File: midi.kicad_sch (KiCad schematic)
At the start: 9 parts, among them J7 MIDI Out 1, J8 MIDI In 1

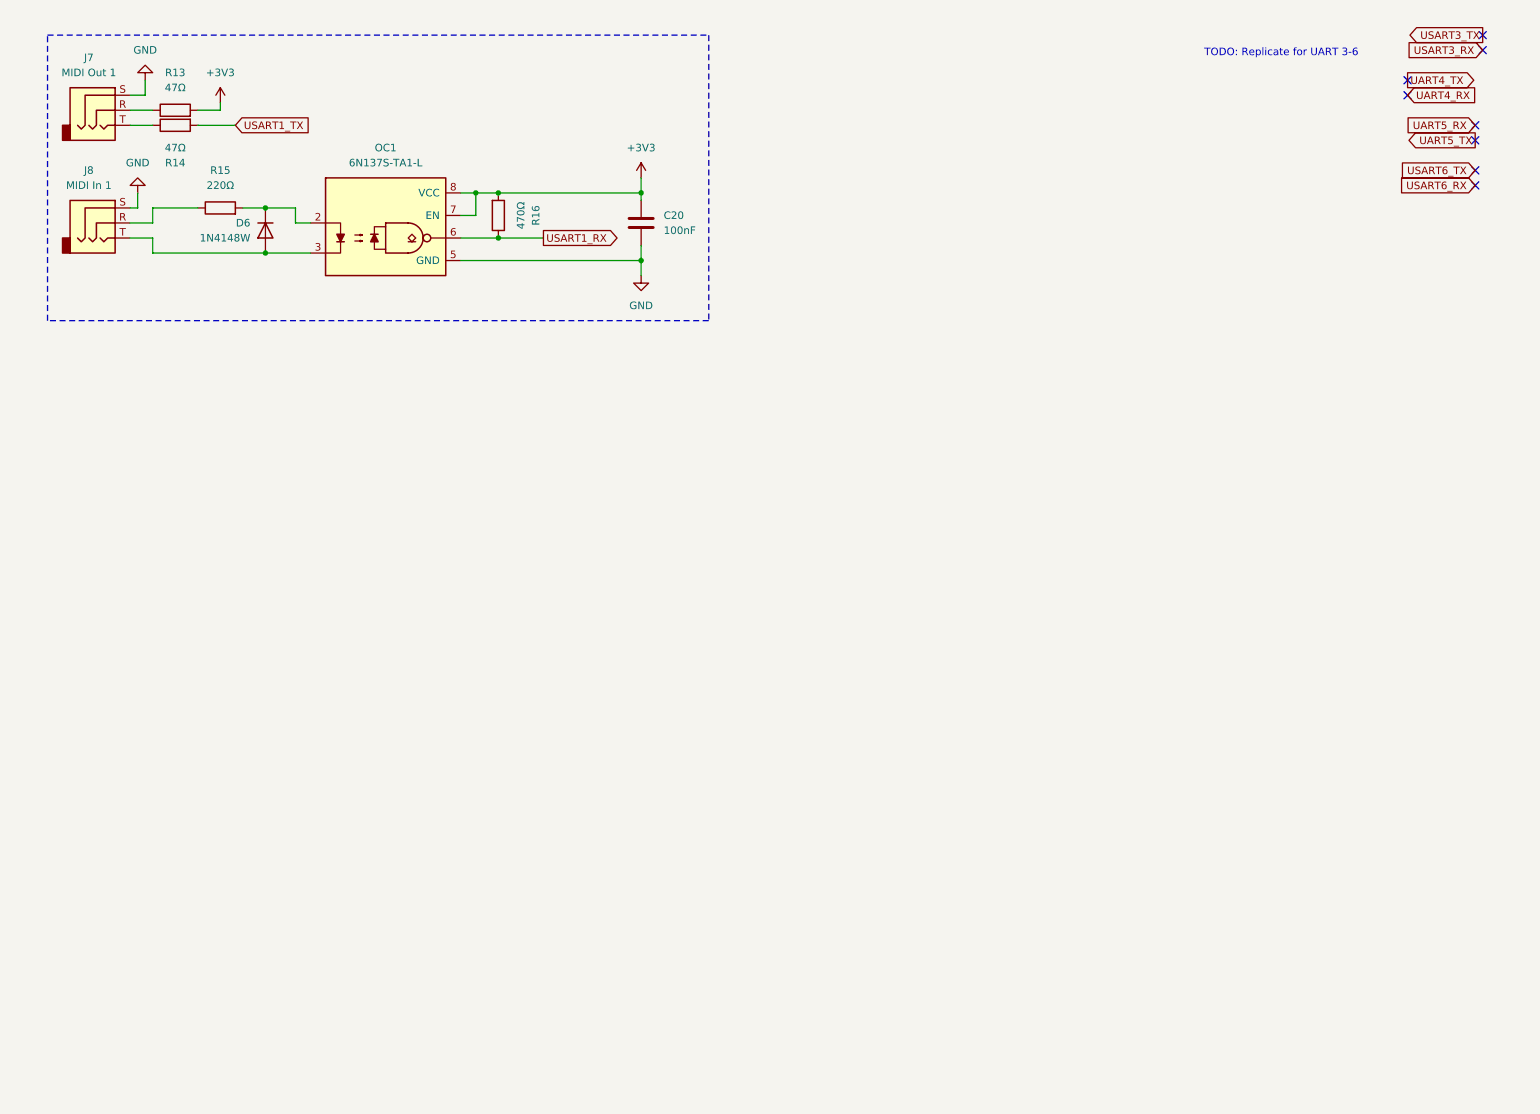
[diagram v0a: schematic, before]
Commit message: Updated schematic with parts found in JLCPCB parts database. Updated footprints, 3d models for those items. All schematic symbols now have LCSC part numbers, footprints and 3D models. No PCB layout has been done.
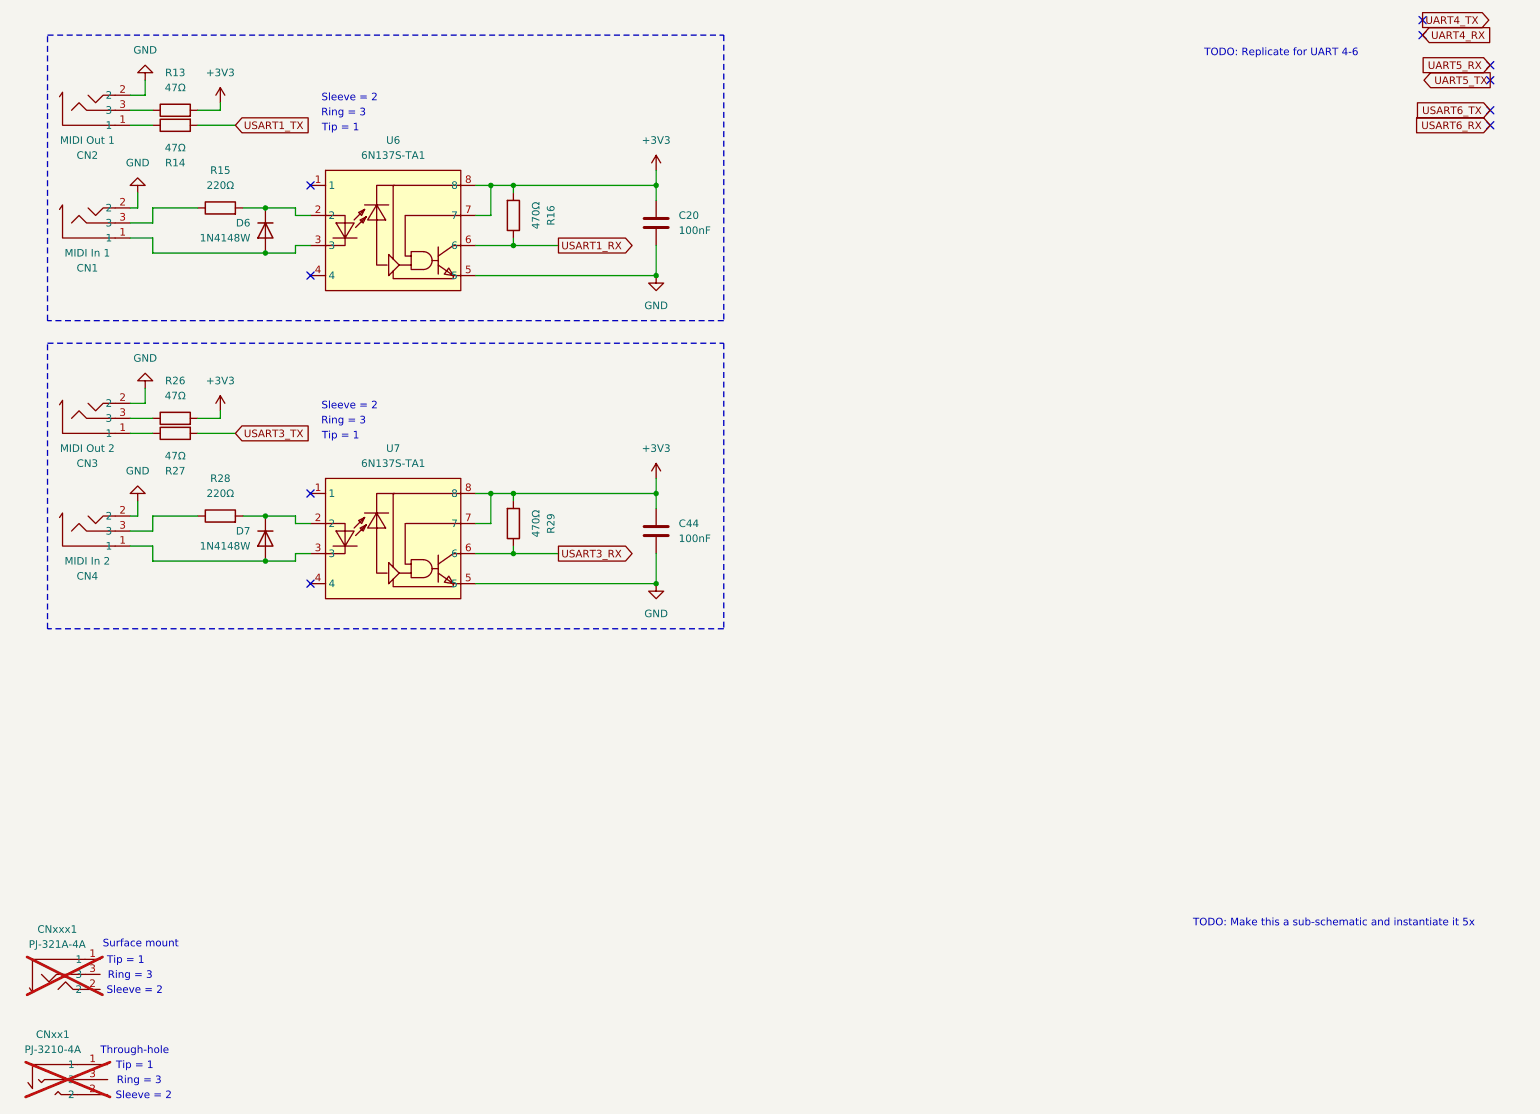
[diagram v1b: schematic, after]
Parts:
- removed J7: MIDI Out 1, symbol Connector_Audio:AudioJack3
- removed J8: MIDI In 1, symbol Connector_Audio:AudioJack3
- removed OC1: 6N137S-TA1-L, PCM_Package_DIP_AKL:SMDIP-8_W9.53mm, symbol PCM_Optocoupler_Logic_AKL:6N137-X007T
- added C44: 100nF, Capacitor_SMD:C_0402_1005Metric, symbol Device:C
- added CN1: MIDI In 1, easyeda2kicad:AUDIO-SMD_PJ-321A-4A, symbol easyeda2kicad:PJ-321A-4A
- added CN2: MIDI Out 1, easyeda2kicad:AUDIO-SMD_PJ-321A-4A, symbol easyeda2kicad:PJ-321A-4A
- added CN3: MIDI Out 2, easyeda2kicad:AUDIO-SMD_PJ-321A-4A, symbol easyeda2kicad:PJ-321A-4A
- added CN4: MIDI In 2, easyeda2kicad:AUDIO-SMD_PJ-321A-4A, symbol easyeda2kicad:PJ-321A-4A
- added CNxx1: PJ-3210-4A, easyeda2kicad:AUDIO_TH_PJ-3210-4A, symbol easyeda2kicad:PJ-3210-4A
- added CNxxx1: PJ-321A-4A, easyeda2kicad:AUDIO-SMD_PJ-321A-4A, symbol easyeda2kicad:PJ-321A-4A
- added D7: 1N4148W, Diode_SMD:D_SOD-123, symbol Diode:1N4148W
- added R26, R27: 47Ω, Resistor_SMD:R_0402_1005Metric, symbol Device:R
- added R28: 220Ω, Resistor_SMD:R_0402_1005Metric, symbol Device:R
- added R29: 470Ω, Resistor_SMD:R_0402_1005Metric, symbol Device:R
- added U6, U7: 6N137S-TA1, easyeda2kicad:SOP-8_L9.8-W6.6-P2.54-LS10.3-BL, symbol easyeda2kicad:6N137S-TA1
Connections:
- net +3V3: now also C44.1, R26.2, R29.2, U6.7, U6.8, U7.7, U7.8
- net GND: now also C44.2, CN1.2, CN2.2, CN3.2, CN4.2, U6.5, U7.5
- net USART1_RX: now also U6.6
- net USART3_RX: now also R29.1, U7.6
- net USART3_TX: now also R27.2
- net at D6.1 (K), R15.2: now also U6.2
- net at D6.2 (A): now also CN1.1, U6.3
- net at R15.1: now also CN1.3
- net at R13.1: now also CN2.3
- net at R14.1: now also CN2.1
- new net: CN3.1, R27.1
- new net: CN3.3, R26.1
- new net: D7.1 (K), R28.2, U7.2
- new net: CN4.1, D7.2 (A), U7.3
- new net: CN4.3, R28.1
- no-connect marks 8 -> 10
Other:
- note added: "Ring = 3"
- note added: "Sleeve = 2"
- note added: "Surface mount"
- note added: "TODO: Make this a sub-schematic and instantiate it 5x"
- note added: "TODO: Replicate for UART 4-6"
- note added: "Through-hole"
- note added: "Tip = 1"
- note removed: "TODO: Replicate for UART 3-6"
- moved on the sheet: C20, R16

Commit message: Move related PCB components near each other in preparation of PCB layout.
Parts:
- renumbered CN2 to CN1, CN1 to CN2
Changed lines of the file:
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@@
 		(on_board yes)
 		(dnp no)
-		(property "Reference" "CN1"
+		(property "Reference" "CN2"
 			(at 27.05 58.42 0)
 			(effects
@@
 			(project "stm-midi-poc1"
 				(path "/7cd74113-1f92-4dcc-8610-19aa9fc81e5f/d4c8579f-7658-4ad2-a672-2baa765565aa"
-					(reference "CN1")
+					(reference "CN2")
 					(unit 1)
 				)
@@
 		(on_board yes)
 		(dnp no)
-		(property "Reference" "CN2"
+		(property "Reference" "CN1"
 			(at 27.05 39.37 0)
 			(effects
@@
 			(project "stm-midi-poc1"
 				(path "/7cd74113-1f92-4dcc-8610-19aa9fc81e5f/d4c8579f-7658-4ad2-a672-2baa765565aa"
-					(reference "CN2")
-					(unit 1)
-				)
+					(reference "CN1")
+					(unit 1)
+				)

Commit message: Group PCB components together more. Replace 2x2x4 by 1x2x8 connector.
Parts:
- added J4: UART456, Connector_PinHeader_2.54mm:PinHeader_2x04_P2.54mm_Vertical, symbol PCM_SL_Pin_Headers:PINHD_2x4_Male
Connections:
- net +3V3: now also J4.7
- net GND: now also J4.8
- net UART4_RX: now also J4.2
- net UART4_TX: now also J4.1
- net UART5_RX: now also J4.4
- net UART5_TX: now also J4.3
- net USART6_RX: now also J4.6
- net USART6_TX: now also J4.5
- no-connect marks 10 -> 4

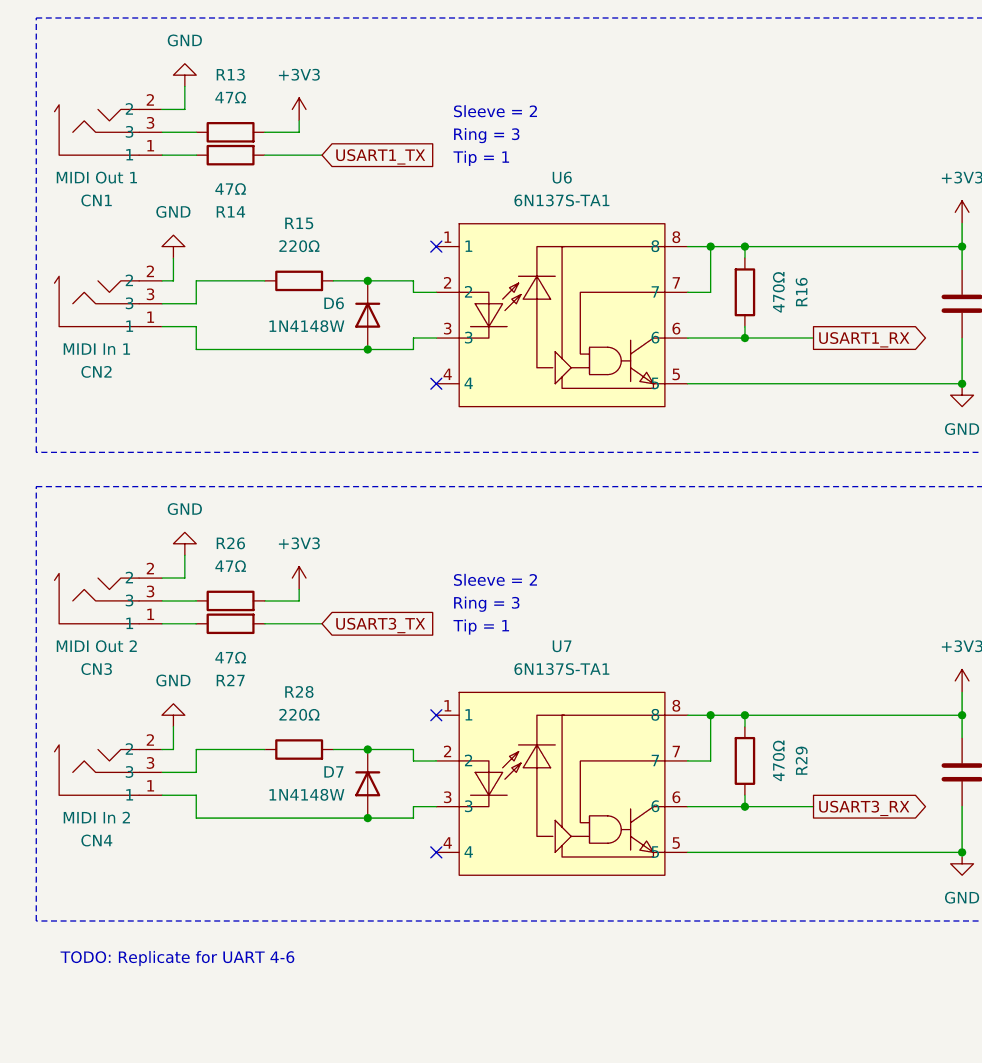
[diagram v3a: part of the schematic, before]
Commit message: Create PCB outline and move components into better locations. (Not done yet!) Update schematic a little bit with additional nets and clarifications. Add mounting holes. Unify components/footprints.
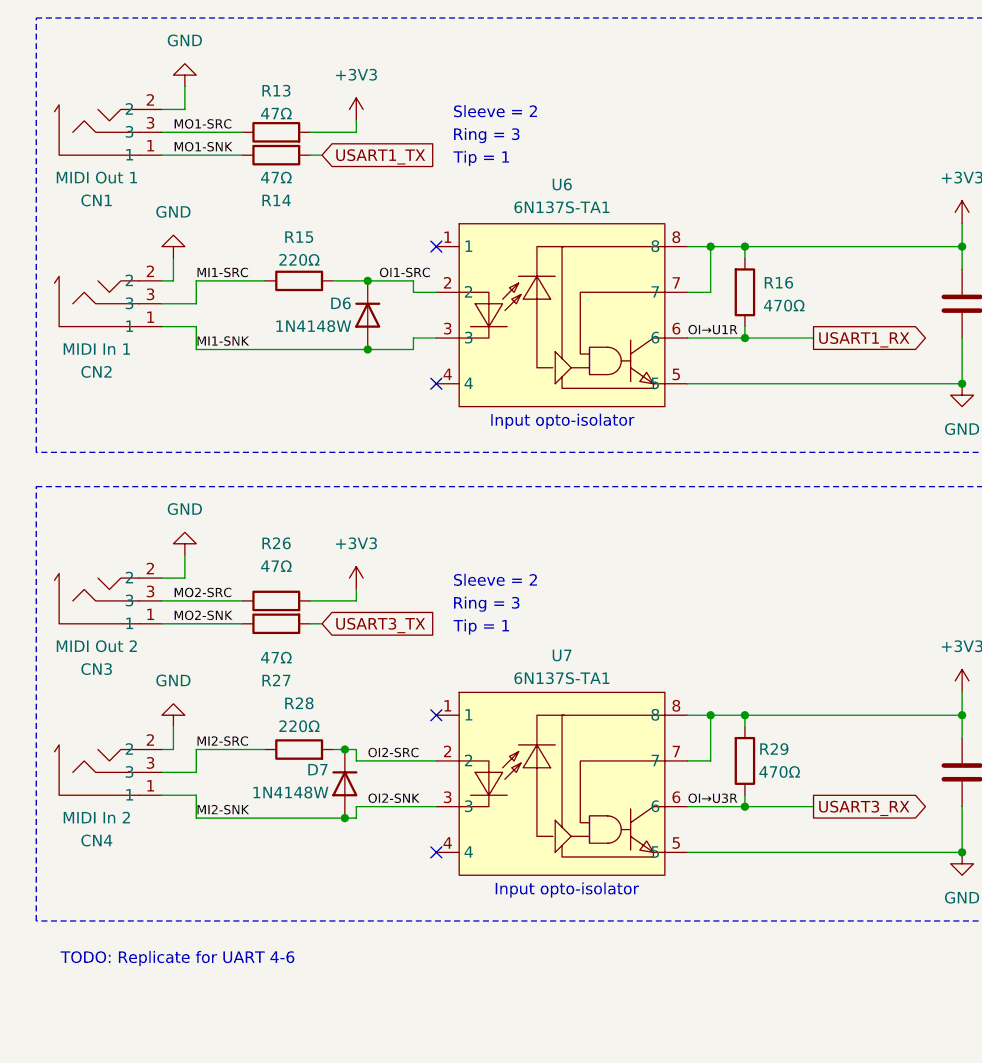
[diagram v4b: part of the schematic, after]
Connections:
- net MO2-SNK: now reaches CN3.1, R27.1
- net MO2-SRC: now reaches CN3.3, R26.1
- net MI1-SNK: now reaches CN2.1, D6.2 (A), U6.3
- net MI1-SRC: now reaches CN2.3, R15.1
- net OI2-SRC: now reaches D7.1 (K), R28.2, U7.2
- net MI2-SNK: now reaches CN4.1, D7.2 (A), U7.3
- net OI1-SRC: now reaches D6.1 (K), R15.2, U6.2
- net MO1-SRC: now reaches CN1.3, R13.1
- net MI2-SRC: now reaches CN4.3, R28.1
- net MO1-SNK: now reaches CN1.1, R14.1
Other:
- note added: "Input opto-isolator"
- moved on the sheet: D7, R13, R14, R26, R27

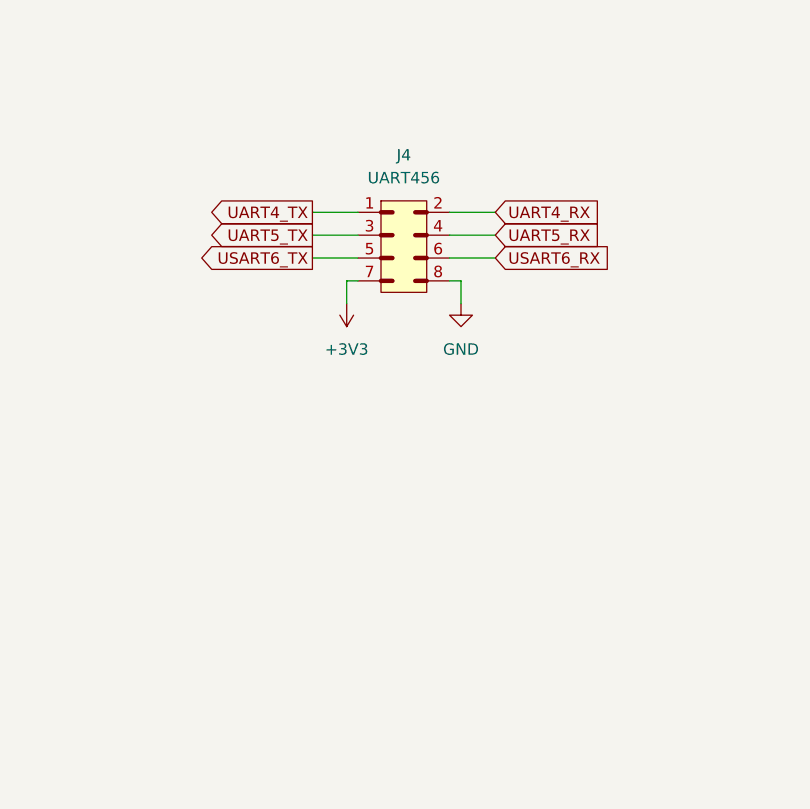
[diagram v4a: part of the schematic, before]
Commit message: All signals now routed through revised GPIO pinout. TODO: Put ground vias everywhere needed for signal vias.
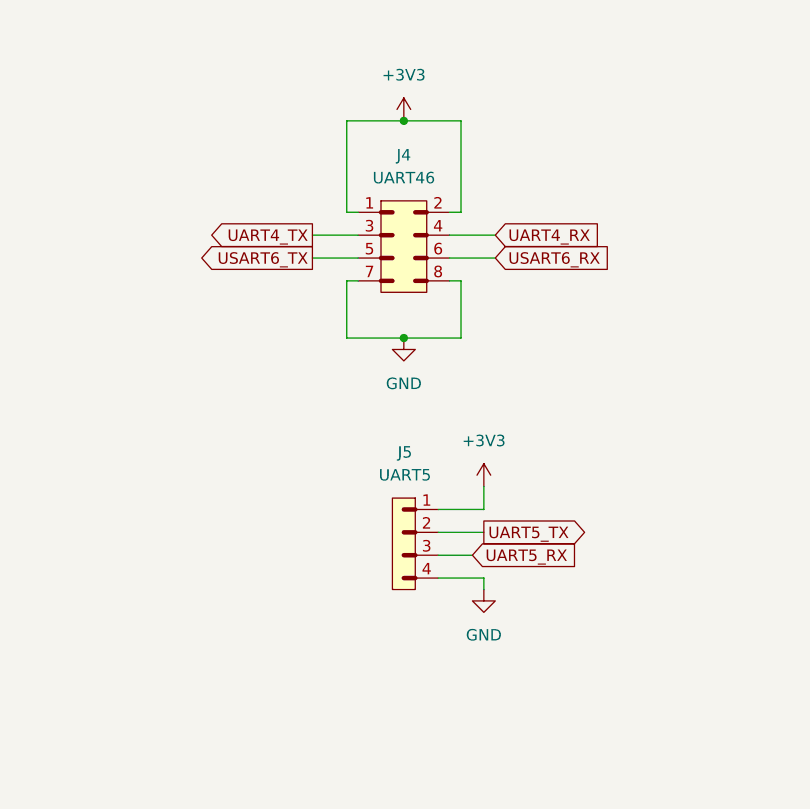
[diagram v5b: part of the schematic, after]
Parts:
- added J5: UART5, Connector_PinHeader_2.54mm:PinHeader_1x04_P2.54mm_Vertical, symbol PCM_SL_Pin_Headers:PINHD_1x4_Male
- J4: value UART456 -> UART46
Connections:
- net +3V3: now also J4.1, J4.2, J5.1; no longer J4.7
- net GND: now also J4.7, J5.4
- net UART4_RX: now also J4.4; no longer J4.2
- net UART4_TX: now also J4.3; no longer J4.1
- net UART5_RX: now also J5.3; no longer J4.4
- net UART5_TX: now also J5.2; no longer J4.3
